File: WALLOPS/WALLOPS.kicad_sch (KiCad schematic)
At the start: 30 parts, among them J1 JST-PH 1x8 Connector from WAL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, U1 VL53L8CX 0 (Zwicky), U2 VL58L8CX 1 (Aristotle), U3 VL53L8CX 3 (Copernicus), U4 VL53L8CX 2 (Brahe), U9 TPS62147RGXR

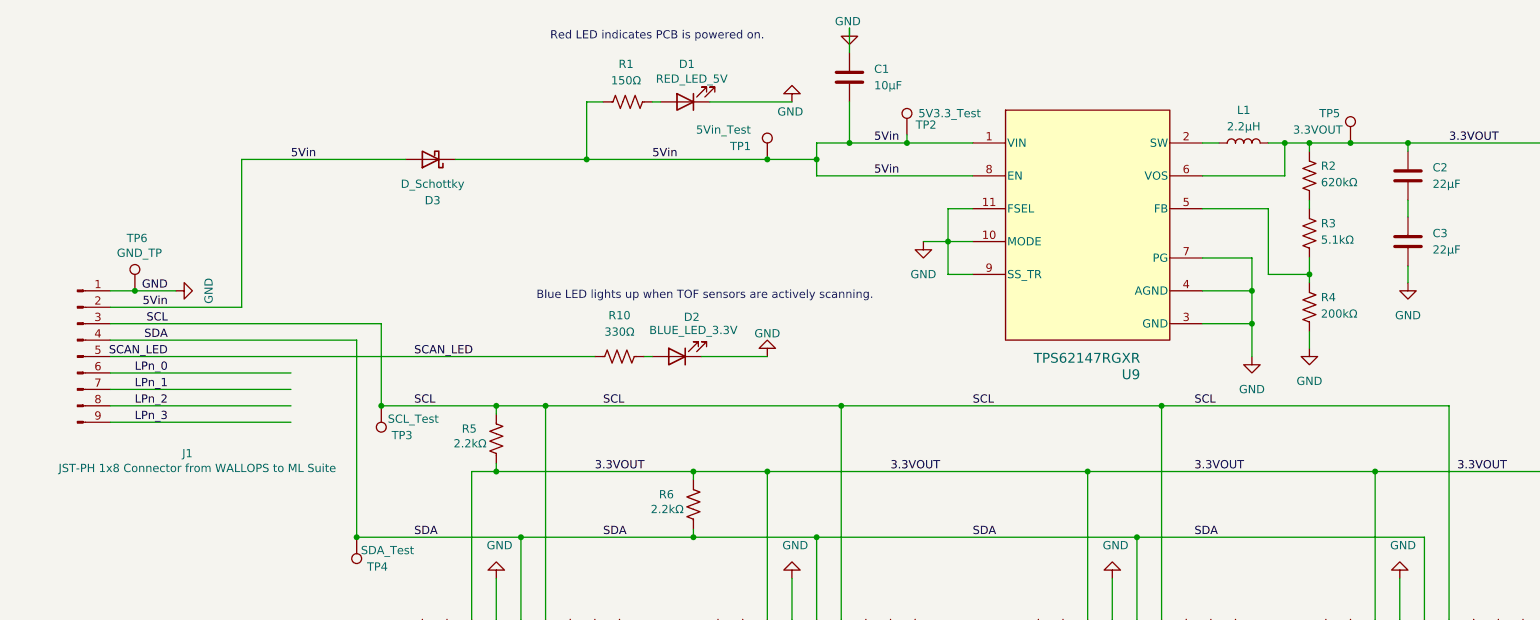
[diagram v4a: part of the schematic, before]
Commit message: Swapped out sch diode with P-MOSFET to fix backflow on 5VIN
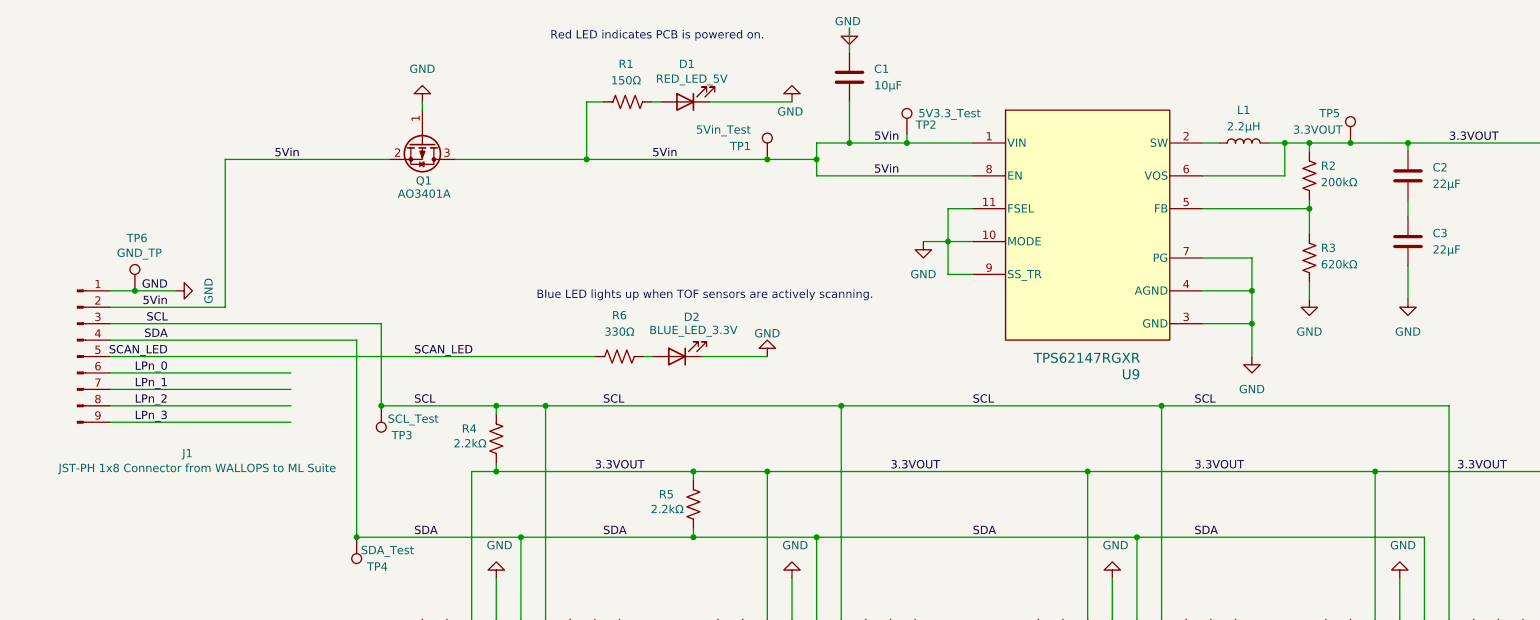
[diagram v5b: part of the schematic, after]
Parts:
- removed D3: D_Schottky, Diode_SMD:D_SMB, symbol Device:D_Schottky
- removed R3: 5.1kΩ, Resistor_SMD:R_0805_2012Metric_Pad1.20x1.40mm_HandSolder, symbol Device:R_US
- added Q1: AO3401A, Package_TO_SOT_SMD:SOT-23_Handsoldering, symbol Transistor_FET:Q_PMOS_GSD
- R2: value 620kΩ -> 200kΩ
- R3: renamed from R4; value 200kΩ -> 620kΩ
- renumbered R5 to R4, R6 to R5, R10 to R6
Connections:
- net 5Vin: now also Q1.2 (S), Q1.3 (D)
- net GND: now also Q1.1 (G)
- net at R3.1, U9.5 (FB): now also R2.2
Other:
- moved on the sheet: R3

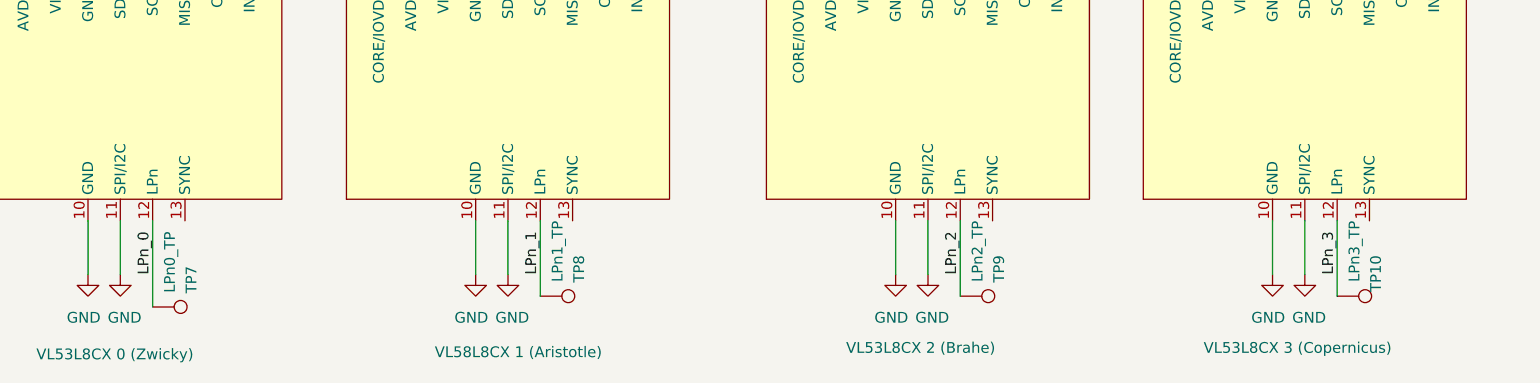
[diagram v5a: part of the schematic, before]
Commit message: Removed extraneous test pins
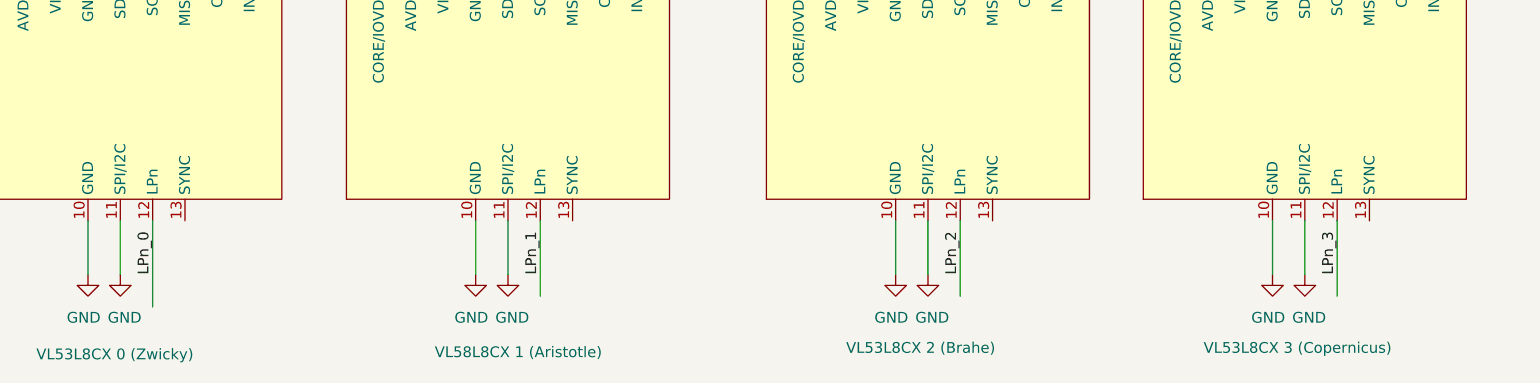
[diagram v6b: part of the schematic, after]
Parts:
- removed TP10: LPn3_TP, TestPoint:TestPoint_Pad_D2.0mm, symbol Connector:TestPoint
- removed TP7: LPn0_TP, TestPoint:TestPoint_Pad_D2.0mm, symbol Connector:TestPoint
- removed TP8: LPn1_TP, TestPoint:TestPoint_Pad_D2.0mm, symbol Connector:TestPoint
- removed TP9: LPn2_TP, TestPoint:TestPoint_Pad_D2.0mm, symbol Connector:TestPoint

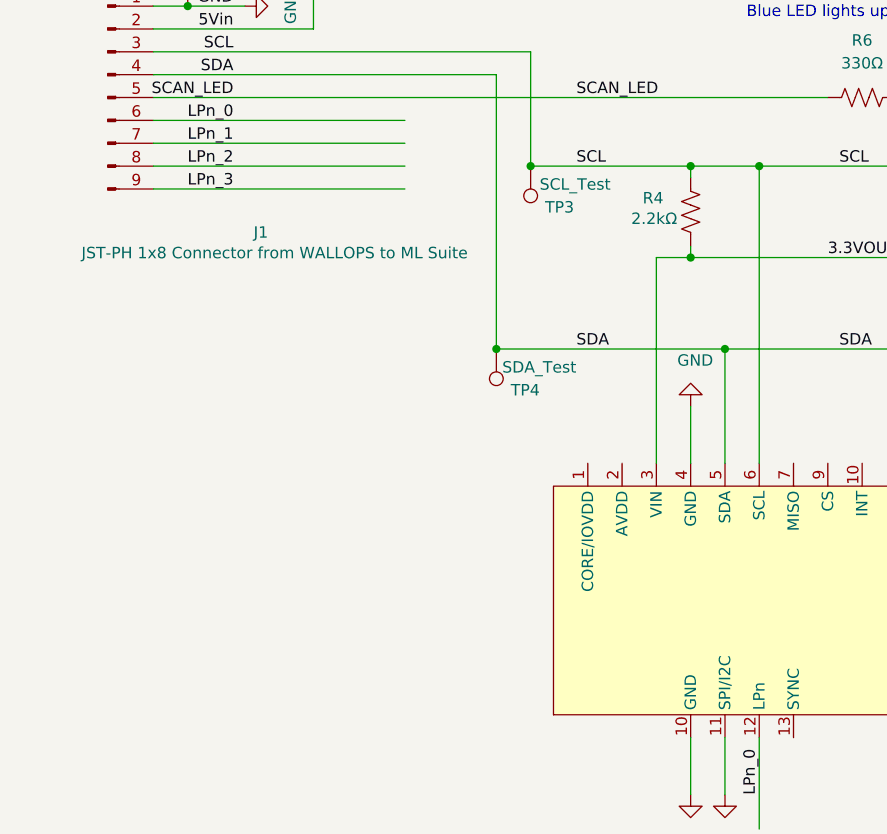
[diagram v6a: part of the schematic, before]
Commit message: Finished first draft of wallops pcb layout
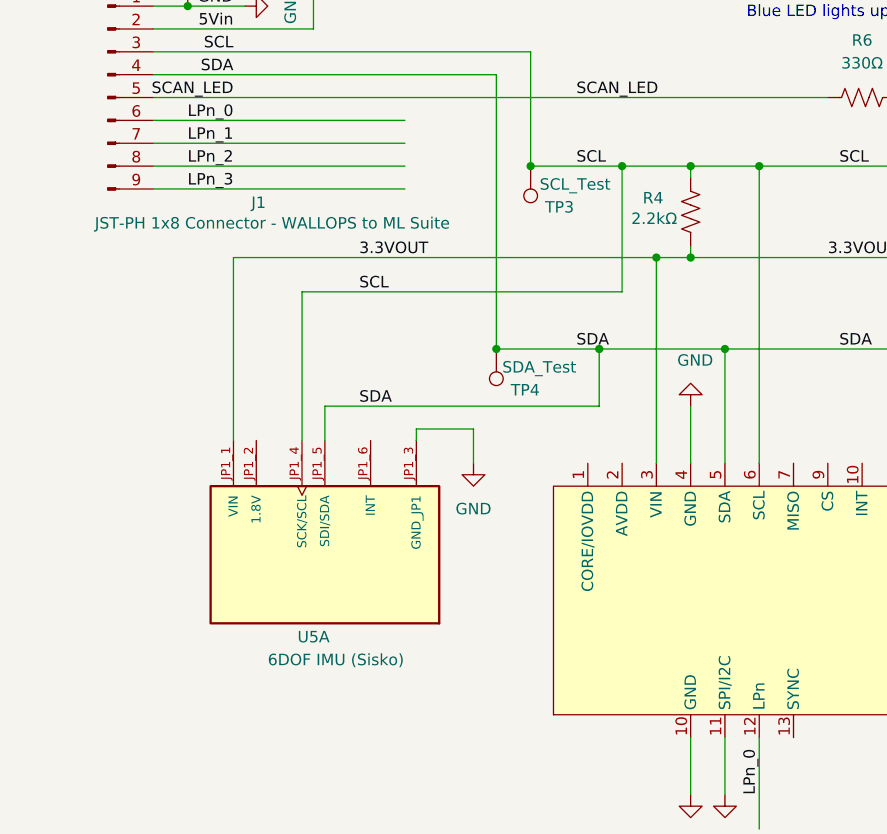
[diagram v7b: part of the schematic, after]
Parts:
- added U5: 6DOF IMU (Sisko), RockSat:6DOF IMU, symbol RockSat_Sym:6DOF IMU
- J1: value JST-PH 1x8 Connector from WALLOPS to ML Suite -> JST-PH 1x8 Connector - WALLOPS to ML Suite
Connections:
- net 3.3VOUT: now also U5.JP1_1 (VIN)
- net GND: now also U5.JP1_3 (GND_JP1)
- net SCL: now also U5.JP1_4 (SCK/SCL)
- net SDA: now also U5.JP1_5 (SDI/SDA)

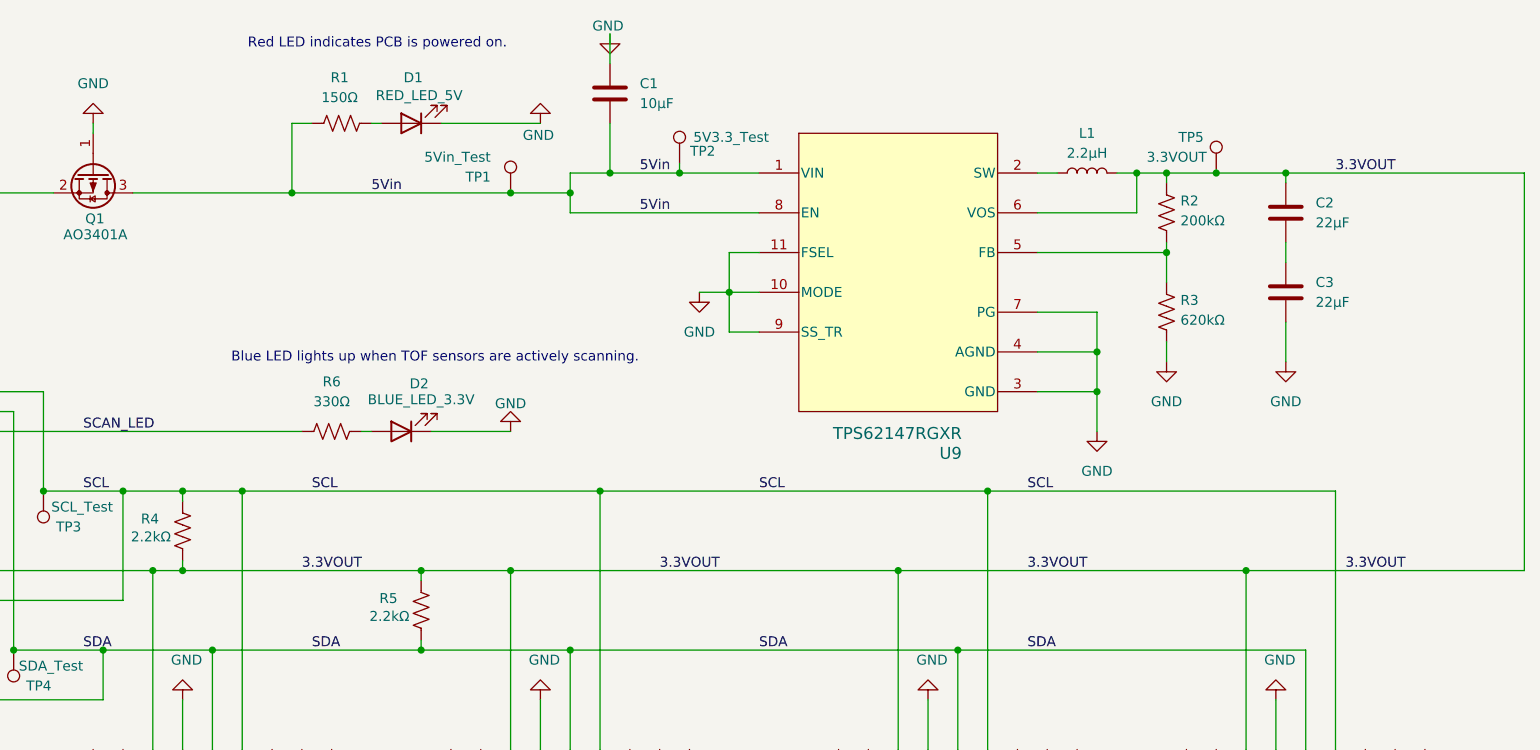
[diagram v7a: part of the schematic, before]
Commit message: Added updated Wallops PCB + schematic
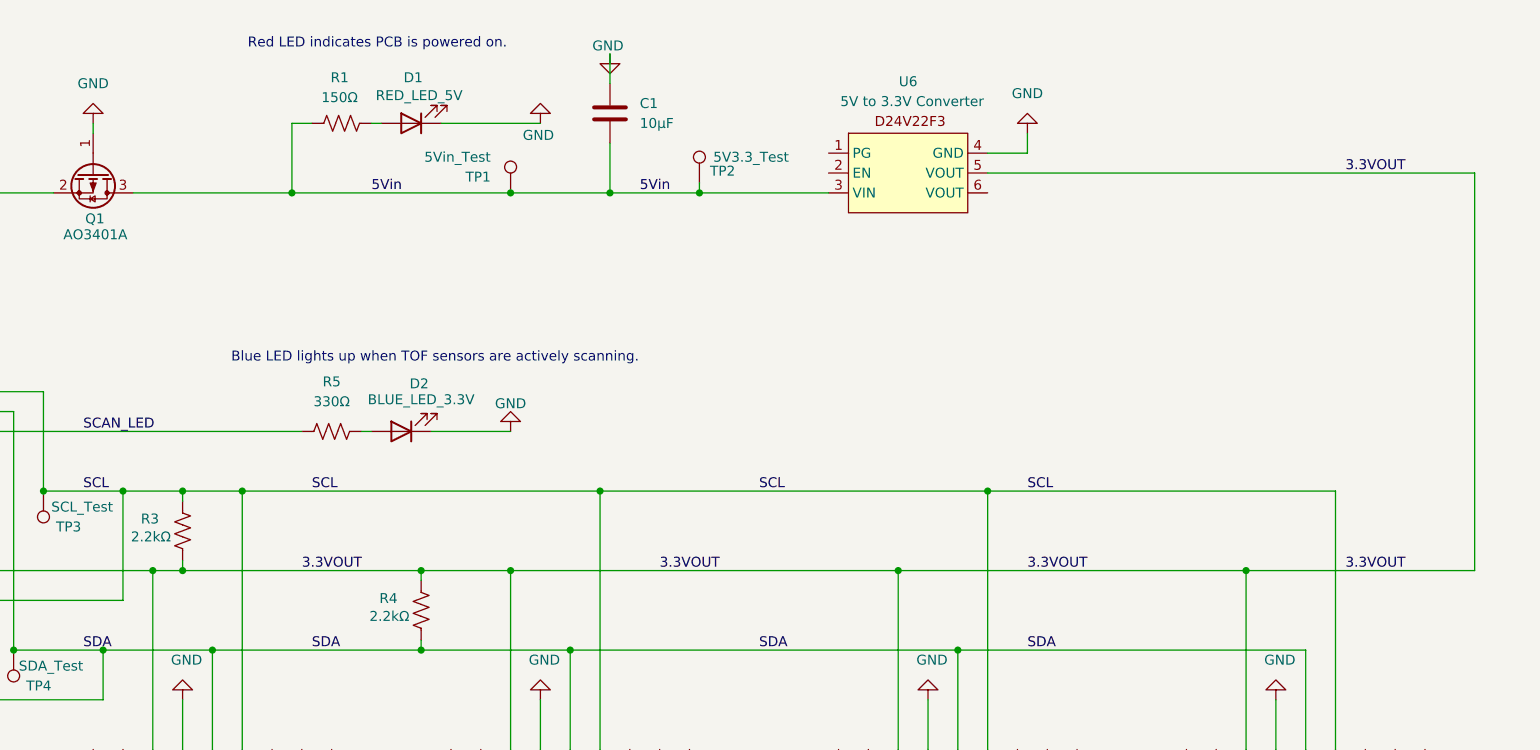
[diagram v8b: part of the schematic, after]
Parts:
- removed C2, C3: 22µF, Capacitor_SMD:C_0805_2012Metric, symbol Device:C
- removed L1: 2.2µH, Inductor_SMD:L_0805_2012Metric, symbol Device:L
- removed R2: 200kΩ, Resistor_SMD:R_0805_2012Metric_Pad1.20x1.40mm_HandSolder, symbol Device:R_US
- removed R3: 620kΩ, Resistor_SMD:R_0805_2012Metric_Pad1.20x1.40mm_HandSolder, symbol Device:R_US
- removed TP5: 3.3VOUT, TestPoint:TestPoint_Pad_D2.0mm, symbol Connector:TestPoint
- removed U9: TPS62147RGXR, RockSat:RGX0011A, symbol RockSat_Sym:TPS62147RGXR
- added U6: 5V to 3.3V Converter, RockSat:D24V22F3, symbol RockSat_Sym:Pololu_D24V22F3
- TP1, TP2, TP3, TP4, TP6: footprint TestPoint:TestPoint_Pad_D2.0mm -> RockSat:TestPoint_Pad_D2.0mm_With_Tolerance
- renumbered R4 to R3, R5 to R4, R6 to R5
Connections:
- net 3.3VOUT: now also U6.5 (VOUT)
- net 5Vin: now also U6.3 (VIN)
- net GND: now also U6.4 (GND)
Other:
- moved on the sheet: C1, TP2
